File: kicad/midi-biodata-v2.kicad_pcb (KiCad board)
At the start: 2 copper layers, 90 x 45.8 mm, 43 parts, among them J1 DIN-5_180degree, J2 PJ-320B, J3 Conn_01x14_Pin, J4 PJ-320B, J5 PJ-320B, J6 PJ-320B, J7 Conn_01x02_Socket, J8 DIN-5_180degree, U1 SN74LVC1G07DBVR, U2 TLP2362TPR_E, U3 LMC555xM, U4 ESP32-S3_SUPERMINI_TH

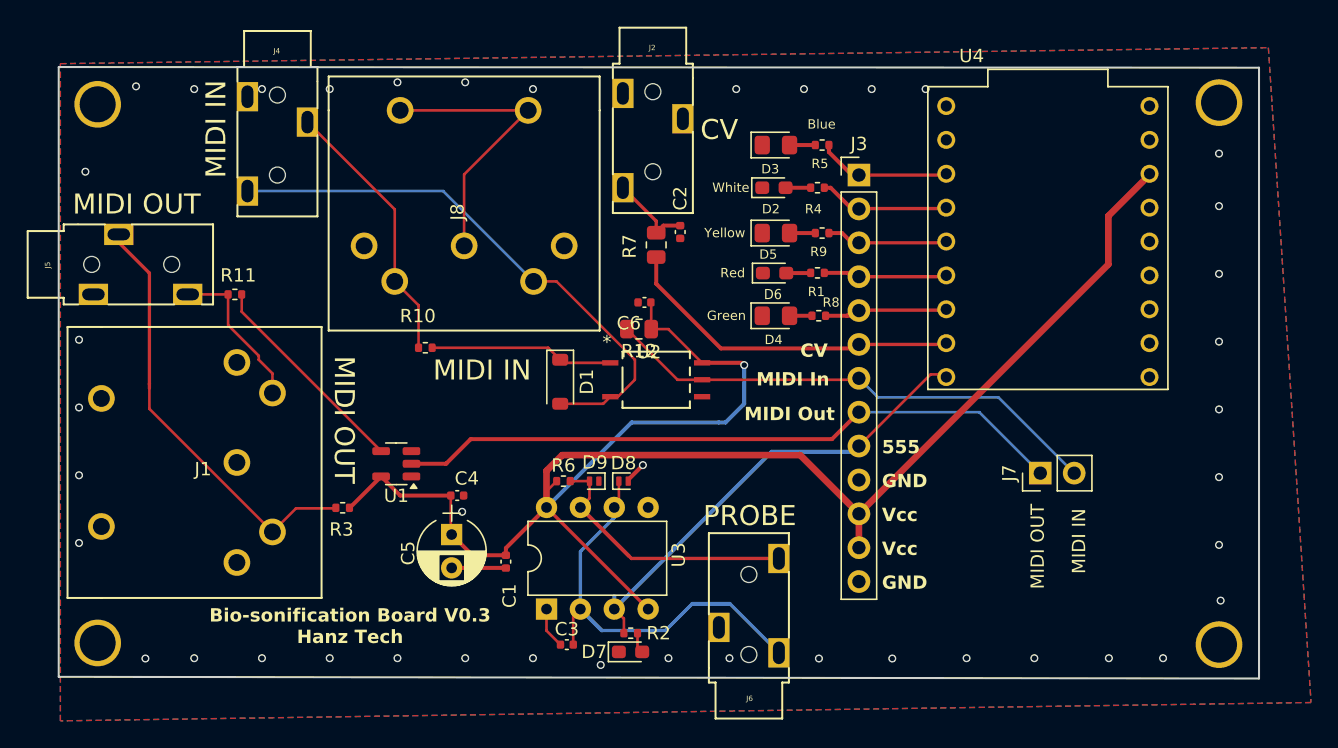
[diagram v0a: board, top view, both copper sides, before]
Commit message: update board to 0.3, add analog partition to board
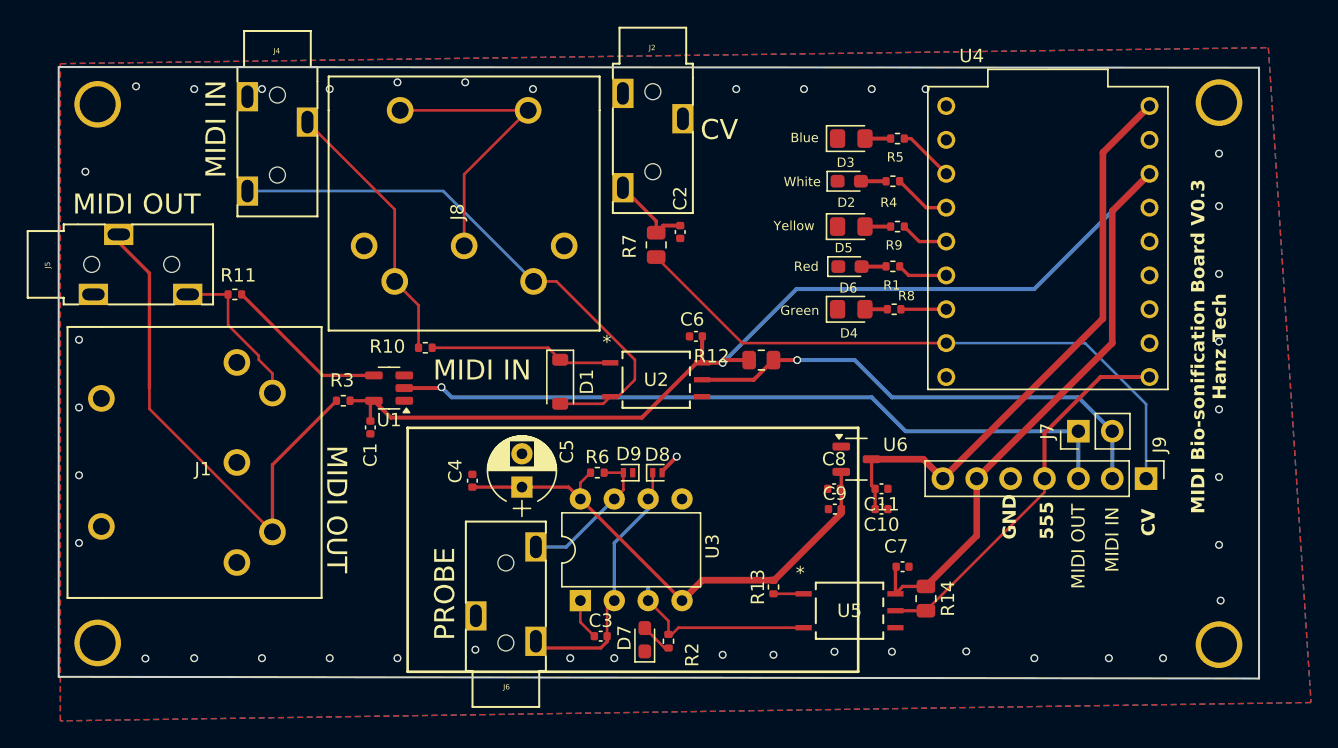
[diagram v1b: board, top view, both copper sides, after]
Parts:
- removed J3: Conn_01x14_Pin, Connector_PinHeader_2.54mm:PinHeader_1x13_P2.54mm_Vertical
- added C10: 0.1uF, Capacitor_SMD:C_0402_1005Metric, F.Cu at (61.7, -12.7)
- added C11: 4.7uF, Capacitor_SMD:C_0402_1005Metric, F.Cu at (61.7, -14.2)
- added C7: 0.1uF, Capacitor_SMD:C_0402_1005Metric, F.Cu at (63.3, -8.38)
- added C8: 0.1uF, Capacitor_SMD:C_0402_1005Metric, F.Cu at (58.1, -14.2)
- added C9: 4.7uF, Capacitor_SMD:C_0402_1005Metric, F.Cu at (58.2, -12.7)
- added J9: Conn_01x07_Pin, Connector_PinHeader_2.54mm:PinHeader_1x07_P2.54mm_Vertical, F.Cu at (81.5, -15.0)
- added R13: 220R, Resistor_SMD:R_0402_1005Metric, F.Cu at (53.6, -6.86)
- added R14: 4.7K, Resistor_SMD:R_0805_2012Metric, F.Cu at (65.0, -5.99)
- added U5: TLP2362TPR_E, poma:tlp2362, F.Cu at (59.3, -5.08)
- added U6: XC6206PxxxMR, Package_TO_SOT_SMD:SOT-23-3, F.Cu at (59.8, -16.4)
- moved J6 18.2 mm to (33.5, -2.67)
- moved C1 14.3 mm to (23.4, -18.8)
- moved R12 9.46 mm to (52.7, -23.9), turned to 0 degrees
- moved R3 8.03 mm to (21.3, -20.8)
- moved C5 6.36 mm to (34.7, -14.4), turned to 90 degrees
- moved U1 5.70 mm to (24.8, -21.8)
- moved D2 5.67 mm to (59.3, -37.3)
- moved D3 5.67 mm to (59.4, -40.5)
- moved D4 5.67 mm to (59.4, -27.7)
- moved D5 5.67 mm to (59.4, -33.9)
- moved D6 5.67 mm to (59.3, -30.9)
- moved R1 5.67 mm to (62.5, -30.9)
- moved R4 5.67 mm to (62.5, -37.3)
- moved R5 5.67 mm to (62.9, -40.5)
- moved R8 5.67 mm to (62.6, -27.7)
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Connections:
- C4 pad 2: +3V3 -> +3V3A
- C5 pad 1: +3V3 -> +3V3A
- R6 pad 1: +3V3 -> +3V3A
- U3 pad 4: +3V3 -> +3V3A
- U3 pad 8: +3V3 -> +3V3A
- U4 pad 5V: unconnected-(U4-Pad5V) -> +5V
- U4 pad 8: 555 -> unconnected-(U4-GPIO7-Pad8)
- U4 pad 9: unconnected-(U4-GPIO8-Pad9) -> ISO_OUT_555
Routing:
- net +5V: track 0.00 -> 44.2 mm
- net +3V3A: track 0.00 -> 39.3 mm
- net ISO_OUT_555: track 0.00 -> 29.2 mm
- net CV: track 25.9 -> 46.9 mm
- net 555: track 35.1 -> 14.5 mm
- net +3V3: track 134.4 -> 118.1 mm
- net Net-(D8-A1): track 31.6 -> 19.8 mm
- net Net-(D9-A2): track 20.2 -> 11.1 mm
- net LED_GREEN: track 10.2 -> 3.40 mm
- net Net-(J1-Pad4): track 32.9 -> 39.0 mm
- net LED_BLUE: track 10.3 -> 4.24 mm
- net LED_WHITE: track 10.0 -> 4.31 mm
- net LED_YELLOW: track 9.34 -> 3.65 mm
- net LED_RED: track 9.51 -> 3.81 mm
- net MIDI_OUT: track 51.1 -> 55.5 mm, vias 0 -> 1
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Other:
- board text added: "MIDI Bio-sonification Board V0.3 Hanz Tech"
- board text removed: "Bio-sonification Board V0.3 Hanz Tech"
- board text removed: "MIDI In"
- board text removed: "MIDI Out"
- board text removed: "Vcc"
